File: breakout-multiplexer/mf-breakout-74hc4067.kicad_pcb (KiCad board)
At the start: 2 copper layers, 80 x 80 mm, 44 parts, among them J1 Multiplexer IN, J10 Conn_01x02_Male, J11 Conn_01x02_Male, J12 Conn_01x02_Male, J13 Button09, J14 Conn_01x02_Male, J15 Conn_01x02_Male, J16 Conn_01x02_Male, J17 Conn_01x02_Male, J18 Conn_01x02_Male, J19 Conn_01x02_Male, J2 Multiplexer OUT, J20 Button16, J21 Button17, J22 Conn_01x02_Male, J23 Conn_01x02_Male, J24 Conn_01x02_Male, J25 Conn_01x02_Male, J26 Conn_01x02_Male, J27 Conn_01x02_Male, J28 Button24, J29 Button25, J3 Data 0, J30 Conn_01x02_Male, J31 Conn_01x02_Male, J32 Conn_01x02_Male, J33 Conn_01x02_Male, J34 Conn_01x02_Male, J35 Conn_01x02_Male, J36 Button32, J4 Data 1, J6 Conn_01x02_Male, J7 Conn_01x02_Male, J8 Conn_01x02_Male, J9 Conn_01x02_Male

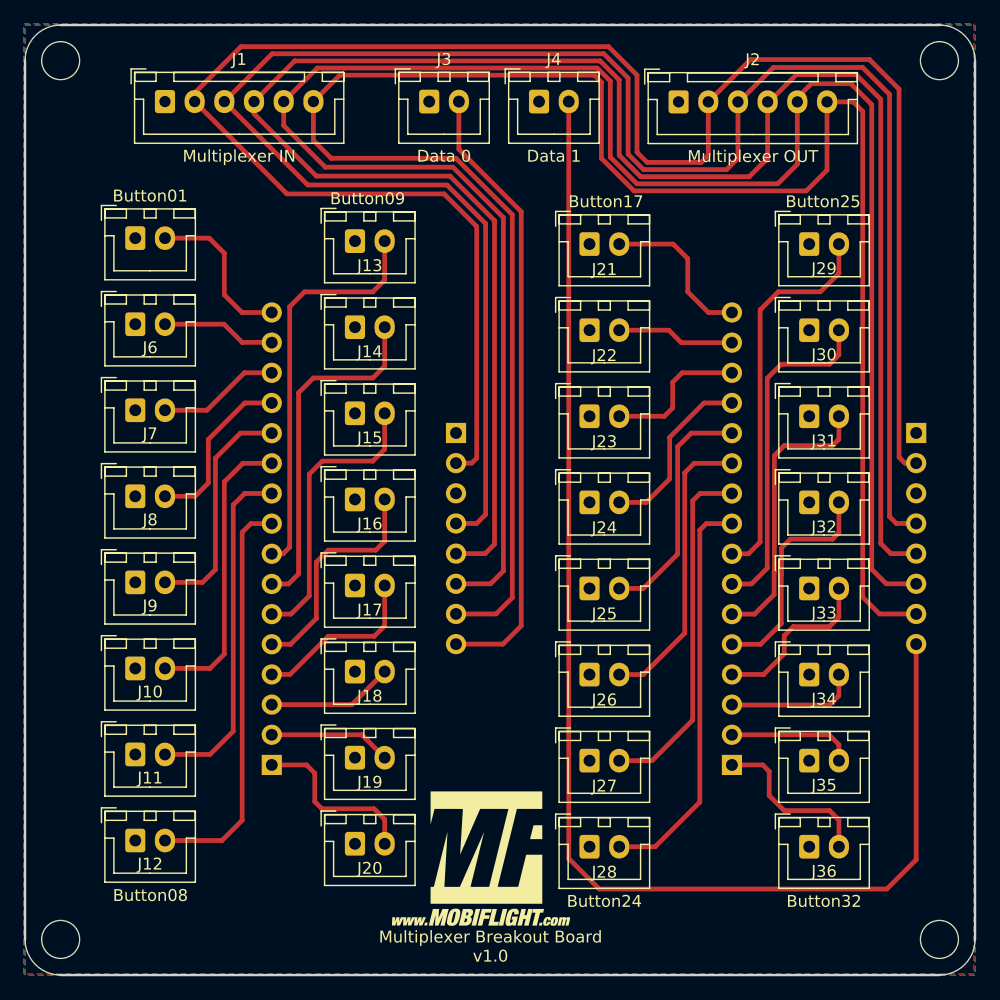
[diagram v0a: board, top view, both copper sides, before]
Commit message: Updated the multiplexer breakout board to v1.2 with better labels, and a QR code
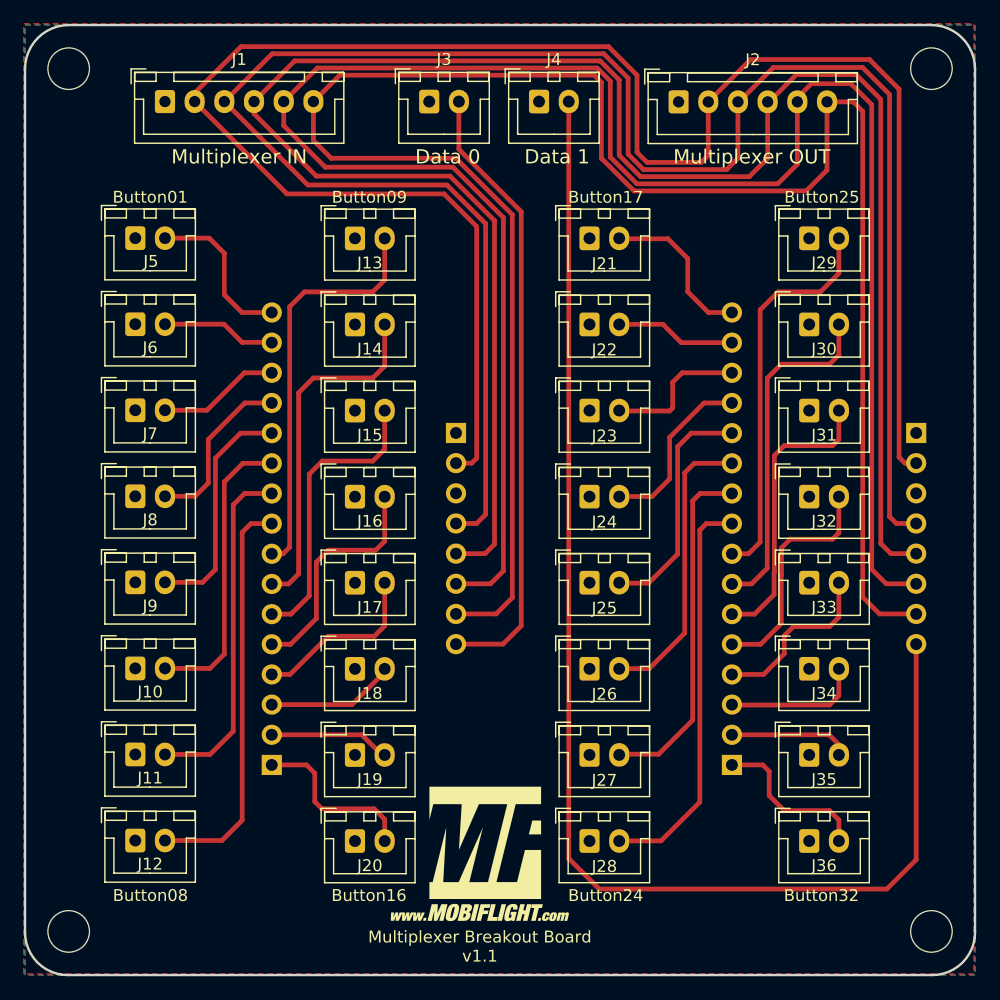
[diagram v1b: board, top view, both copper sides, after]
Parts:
- added G***: LOGO, LOGO, B.Cu at (44.2, 94.6)
- added REF**: CE-Logo_8.5x6mm_SilkScreen, Symbol:CE-Logo_8.5x6mm_SilkScreen, B.Cu at (83.0, 94.2)
- H1, H2, H3, H4: footprint MountingHole:MountingHole_3.2mm_M3 -> MountingHole:MountingHole_3.5mm
- J1: value Multiplexer IN -> Conn_01x06_Male
- J13: value Button09 -> Conn_01x02_Male
- J2: value Multiplexer OUT -> Conn_01x06_Male
- J20: value Button16 -> Conn_01x02_Male
- J21: value Button17 -> Conn_01x02_Male
- J28: value Button24 -> Conn_01x02_Male
- J29: value Button25 -> Conn_01x02_Male
- J3: value Data 0 -> Conn_01x02_Male
- J36: value Button32 -> Conn_01x02_Male
- J4: value Data 1 -> Conn_01x02_Male
- MUX1, MUX2: footprint common:74HC4067 -> footprints:74HC4067
- moved H1 0.95 mm to (28.7, 28.7)
- moved H2 0.95 mm to (101.3, 28.7)
- moved H3 0.95 mm to (28.7, 101.3)
- moved H4 0.95 mm to (101.3, 101.3)
- moved J21 0.48 mm to (72.5, 43.0)
- moved J22 0.48 mm to (72.5, 50.2)
- moved J23 0.48 mm to (72.5, 57.5)
- moved J29 0.48 mm to (91.0, 43.0)
- moved J30 0.48 mm to (91.0, 50.2)
- moved J31 0.48 mm to (91.0, 57.5)
- moved J24 0.48 mm to (72.5, 64.7)
- moved J25 0.48 mm to (72.5, 72.0)
- moved J26 0.48 mm to (72.5, 79.2)
- moved J27 0.48 mm to (72.5, 86.5)
- moved J28 0.48 mm to (72.5, 93.7)
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- renumbered Button01 to J5
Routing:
- net btn22: track 12.3 -> 11.6 mm
- net btn24: track 20.2 -> 19.6 mm
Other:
- outline, holes or cut-outs redrawn
- board text added: "+5V"
- board text added: "B09"
- board text added: "B10"
- board text added: "B11"
- board text added: "B12"
- board text added: "B13"
- board text added: "B14"
- board text added: "B15"
- board text added: "B16"
- board text added: "B17"
- board text added: "B24"
- board text added: "B25"
- board text added: "B32"
- board text added: "B_0"
- board text added: "B_1"
- board text added: "B_2"
- board text added: "B_3"
- board text added: "B_4"
- board text added: "B_5"
- board text added: "B_6"
- board text added: "B_7"
- board text added: "B_8"
- board text added: "B_9"
- board text added: "Button09"
- board text added: "Button16"
- board text added: "Button17"
- board text added: "Button24"
- board text added: "Button25"
- board text added: "Button32"
- board text added: "Data 0"
- board text added: "Data 1"
- board text added: "Data0"
- board text added: "Data1"
- board text added: "E"
- board text added: "GND"
- board text added: "Multiplexer Breakout Board v1.1"
- board text added: "Multiplexer IN"
- board text added: "Multiplexer OUT"
- board text added: "S0"
- board text added: "S1"
- board text added: "S2"
- board text added: "S3"
- board text added: "SIG0"
- board text added: "SIG1"
- board text added: "SIG2"
- board text added: "SIG3"
- board text added: "SIG4"
- board text added: "VCC"
- board text added: "take me to the docs"
- board text removed: "Multiplexer Breakout Board v1.0"

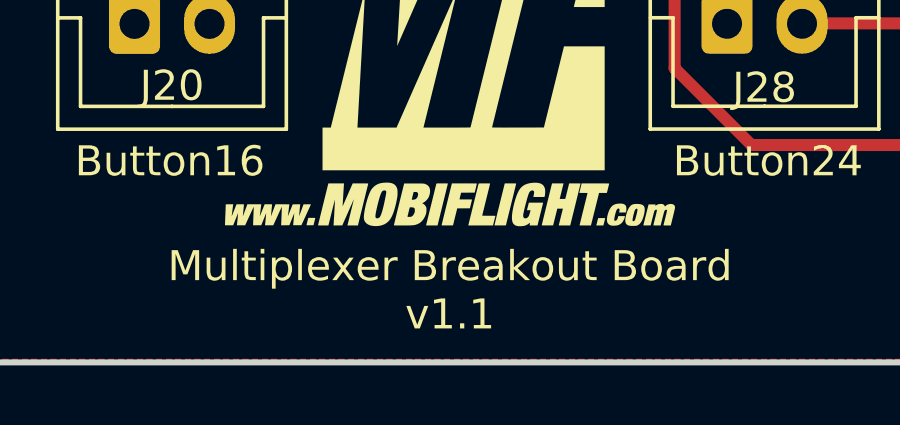
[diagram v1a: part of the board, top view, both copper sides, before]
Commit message: updated label on PCB to v1.2
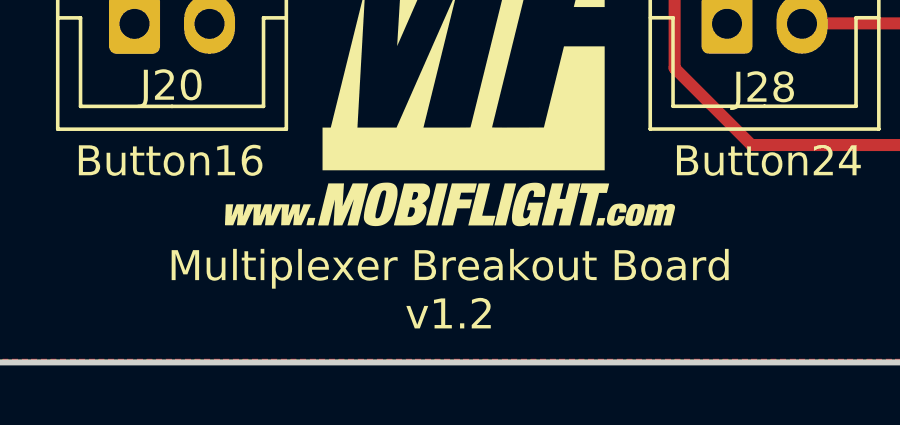
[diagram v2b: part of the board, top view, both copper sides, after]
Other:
- board text added: "Multiplexer Breakout Board v1.2"
- board text removed: "Multiplexer Breakout Board v1.1"
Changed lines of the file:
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@@
     (effects (font (size 1 1) (thickness 0.15)) (justify mirror))
   )
-  (gr_text "Multiplexer Breakout Board\nv1.1" (at 63.283282 102.593145) (layer "B.SilkS")
+  (gr_text "Multiplexer Breakout Board\nv1.2" (at 63.283282 102.593145) (layer "B.SilkS")
     (effects (font (size 1 1) (thickness 0.15)) (justify mirror))
   )
@@
     (effects (font (size 1 1) (thickness 0.15)))
   )
-  (gr_text "Multiplexer Breakout Board\nv1.1" (at 63.299523 102.6) (layer "F.SilkS")
+  (gr_text "Multiplexer Breakout Board\nv1.2" (at 63.299523 102.6) (layer "F.SilkS")
     (effects (font (size 1 1) (thickness 0.15)))
   )

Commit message: multiplexer board v1.4 changes
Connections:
- MUX1 pad 3: unconnected-(MUX1-Pad3) -> pinGnd
- MUX2 pad 3: unconnected-(MUX2-Pad3) -> pinGnd

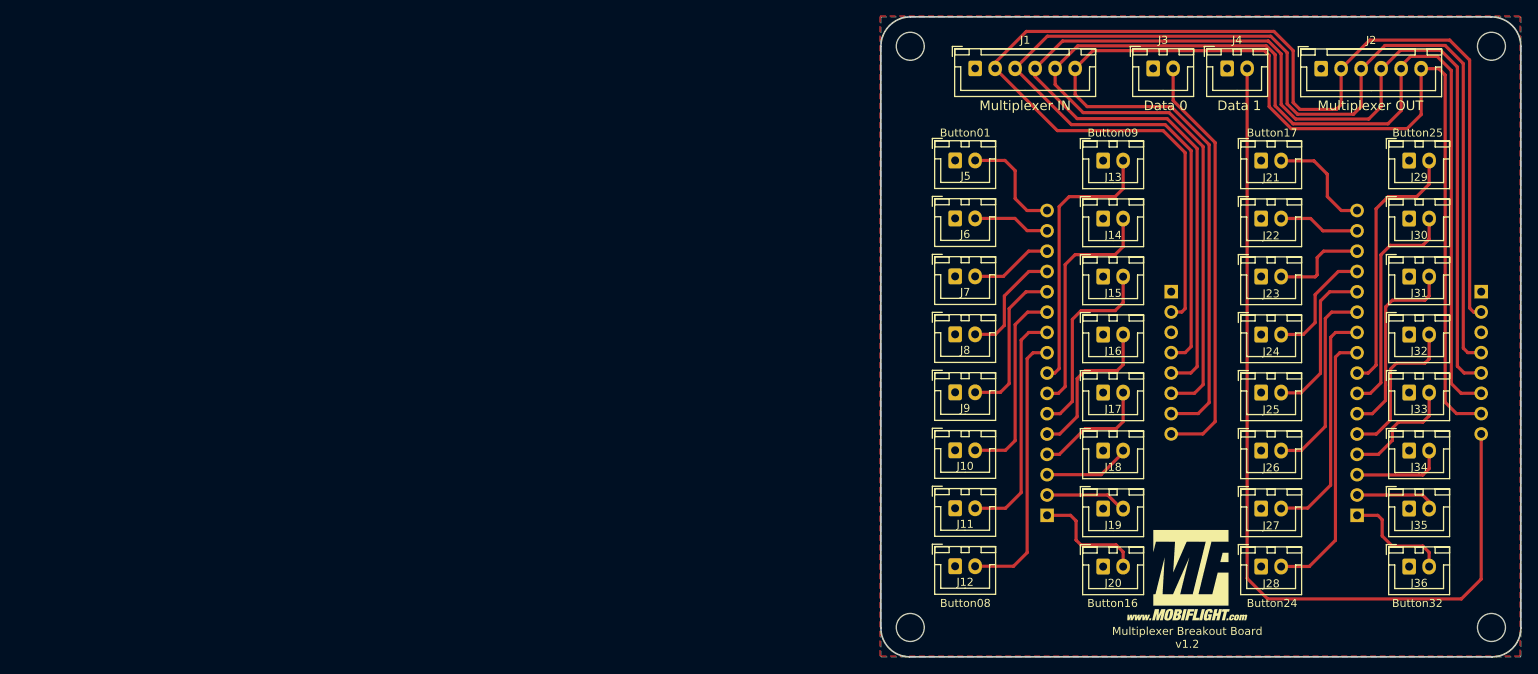
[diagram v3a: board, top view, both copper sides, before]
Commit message: fixed mounting holes and track width
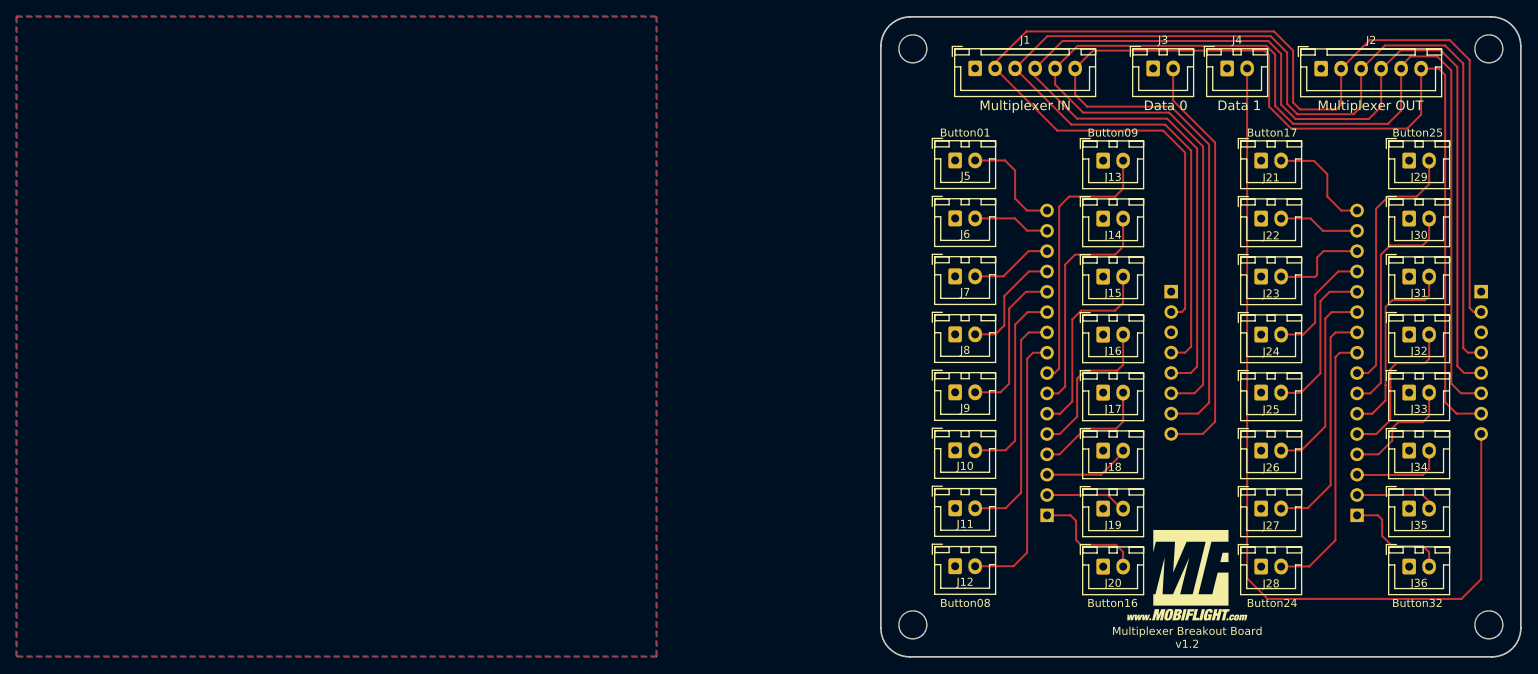
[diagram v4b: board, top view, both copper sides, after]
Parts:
- moved H4 0.46 mm to (101.0, 101.0)
- moved H2 0.46 mm to (101.0, 29.0)
- moved H3 0.46 mm to (29.0, 101.0)
- moved H1 0.46 mm to (29.0, 29.0)

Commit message: Updated 74HC4067 footprints, track size
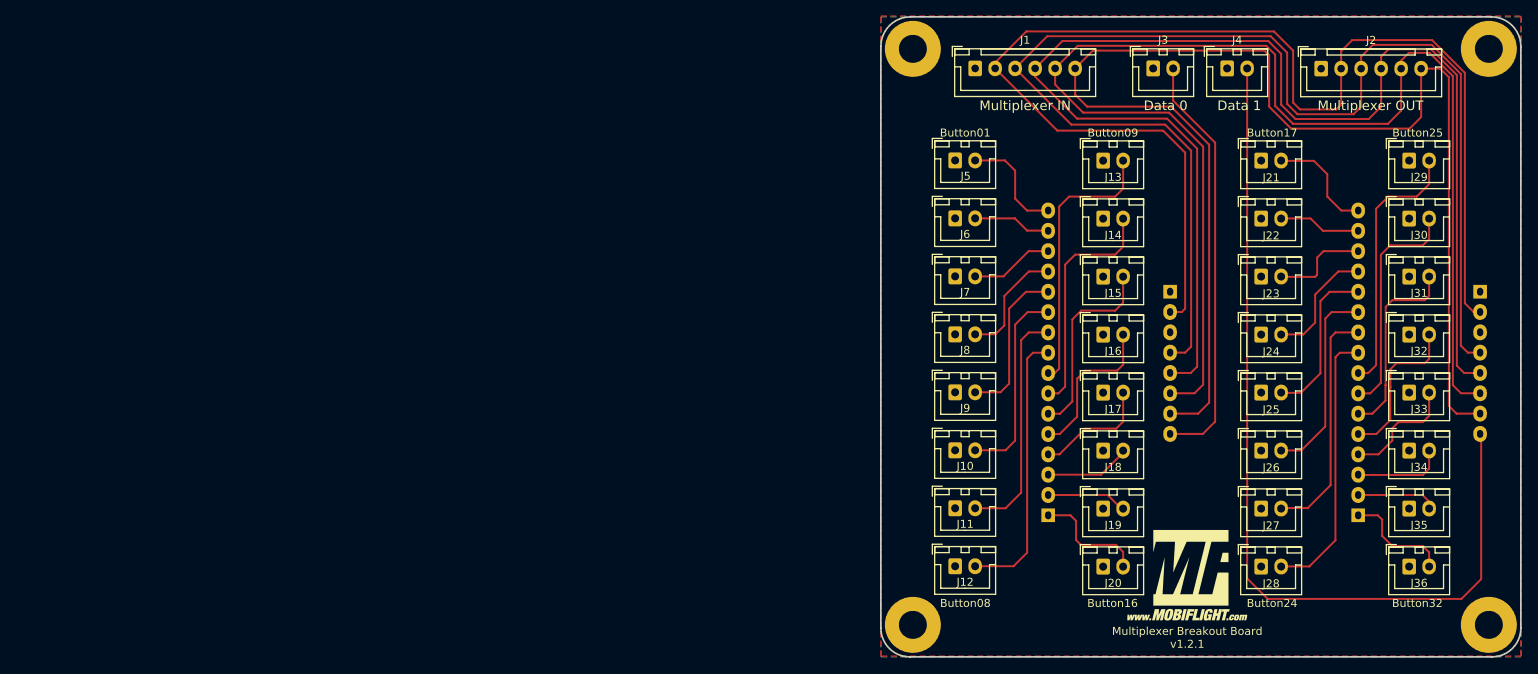
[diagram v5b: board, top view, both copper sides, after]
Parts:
- G*** (x2): footprint common:mobiflight-logo-15 -> MobiFlight:mobiflight-logo-15
- G***: value LOGO -> QR-docs-mux-breakout-board; footprint LOGO -> MobiFlight:QR-docs-mux-breakout-board
- H1, H2, H3, H4: footprint MountingHole:MountingHole_3.5mm -> MountingHole:MountingHole_3.5mm_Pad
- MUX1, MUX2: footprint footprints:74HC4067 -> MobiFlight:74HC4067
- REF**: footprint Symbol:CE-Logo_8.5x6mm_SilkScreen -> MobiFlight:CE-Logo_8.5x6mm_SilkScreen
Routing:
- added copper zone on F.Cu, net pinGnd
- removed copper zone on F.Cu, net (none)
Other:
- board text added: "Multiplexer Breakout Board v1.2.1"
- board text removed: "Multiplexer Breakout Board v1.2"
